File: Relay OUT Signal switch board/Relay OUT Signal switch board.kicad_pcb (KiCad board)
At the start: 2 copper layers, 55 x 75 mm, 18 parts, among them IC1 ULN2003LVDR, J1 1725672, J2 1725672, J3 SE Out, J4 R_Bal_out, J5 Left Bal out, J6 Right 2, J7 Right 1, J8 Left 1, J9 Left 2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

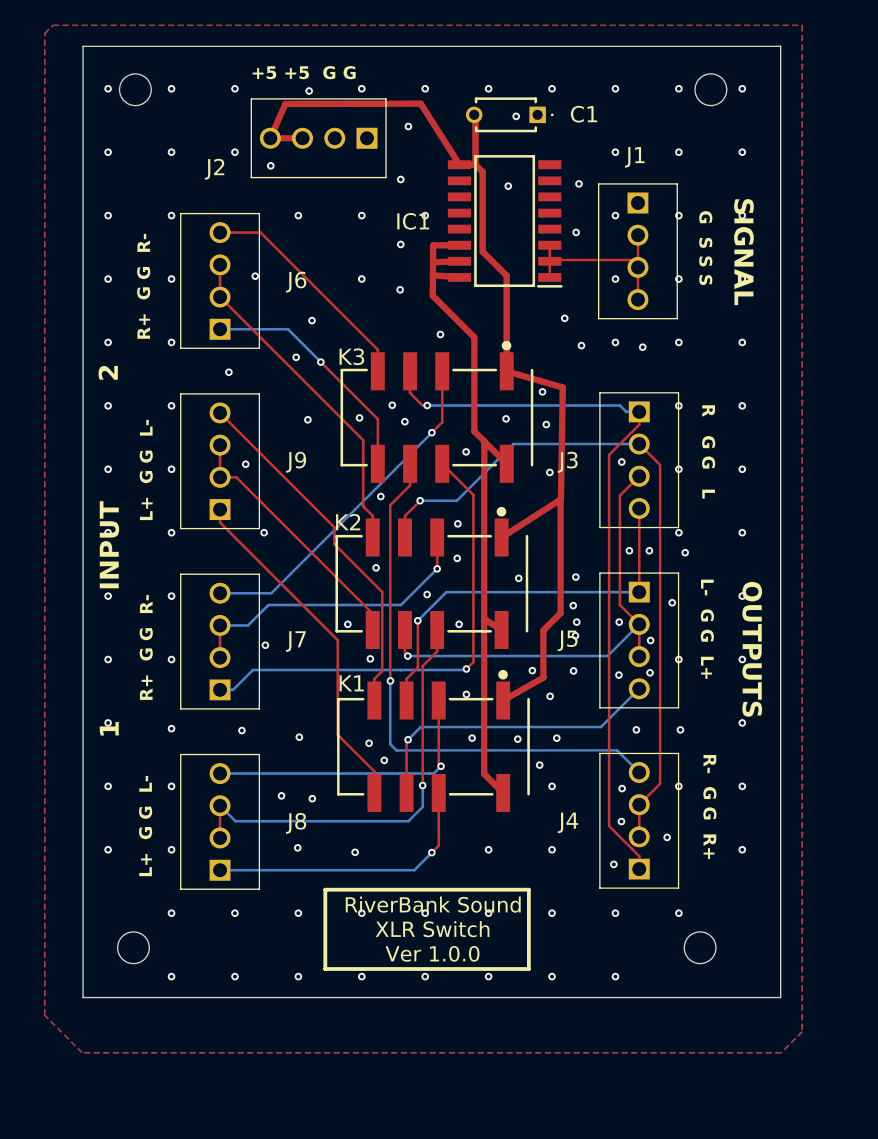
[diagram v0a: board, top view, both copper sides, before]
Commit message: update relayboard set size for RPI4
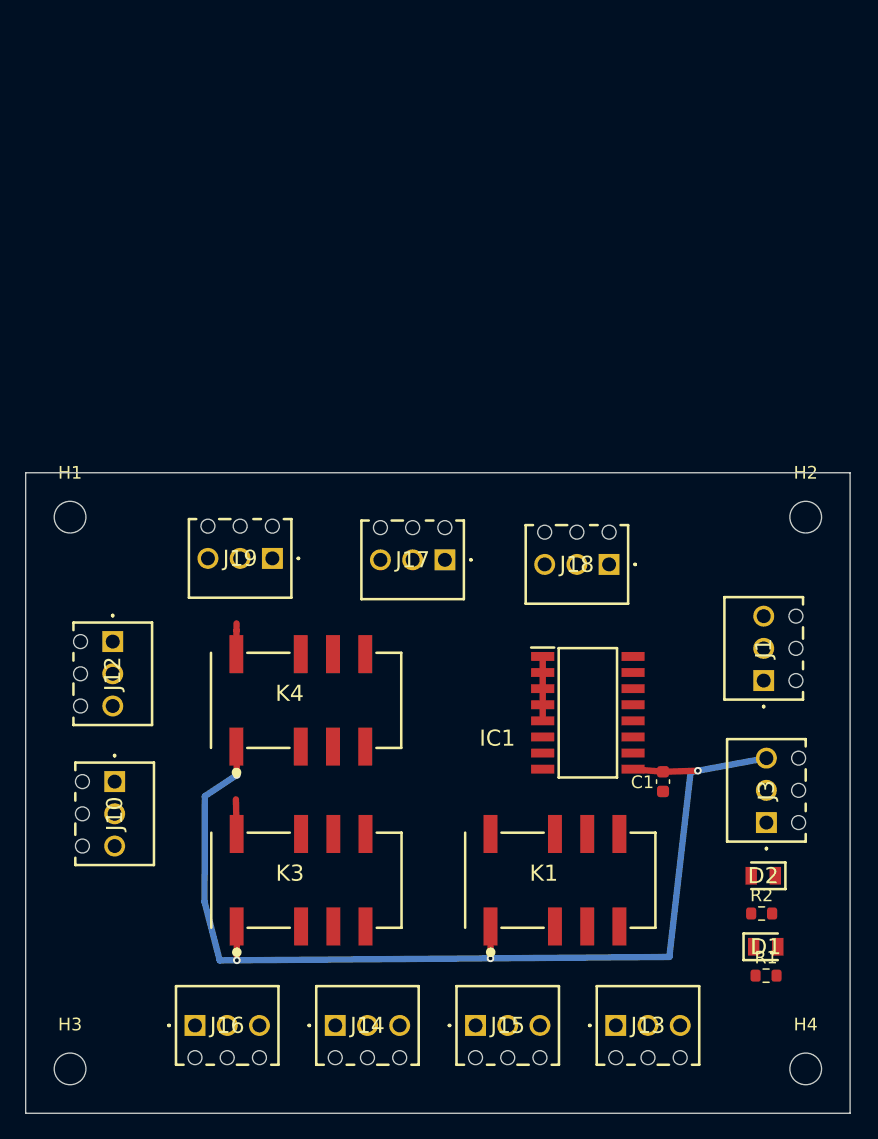
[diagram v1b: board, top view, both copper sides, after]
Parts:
- removed J2: 1725672, samsys:1725672
- removed J4: R_Bal_out, samsys:1725672
- removed J5: Left Bal out, samsys:1725672
- removed J6: Right 2, samsys:1725672
- removed J7: Right 1, samsys:1725672
- removed J8: Left 1, samsys:1725672
- removed J9: Left 2, samsys:1725672
- removed K2: Gnd Relay, samsys:EE2-5NU
- added D1: LS_R976, samsys:LEDC2012X40N, F.Cu at (158.3, 87.4)
- added D2: LS_R976, samsys:LEDC2012X40N, F.Cu at (158.2, 81.8)
- added J10: 1725669, samsys:1725669, F.Cu at (107.0, 74.3)
- added J12: 1725669, samsys:1725669, F.Cu at (106.9, 63.3)
- added J13: 1725669, samsys:1725669, F.Cu at (146.5, 93.6)
- added J14: 1725669, samsys:1725669, F.Cu at (124.4, 93.6)
- added J15: 1725669, samsys:1725669, F.Cu at (135.5, 93.6)
- added J16: 1725669, samsys:1725669, F.Cu at (113.3, 93.6)
- added J17: 1725669, samsys:1725669, F.Cu at (133.1, 56.9)
- added J18: 1725669, samsys:1725669, F.Cu at (146.0, 57.2)
- added J19: 1725669, samsys:1725669, F.Cu at (119.5, 56.8)
- added K4: Left Bal, samsys:EE2-5NU, F.Cu at (114.6, 67.9)
- added R1: 1k, Resistor_SMD:R_0603_1608Metric, F.Cu at (158.4, 89.7)
- added R2: 1k, Resistor_SMD:R_0603_1608Metric, F.Cu at (158.0, 84.8)
- C1: footprint samsys:K104K20X7RK53H5G -> Capacitor_SMD:C_0603_1608Metric
- J1: value 1725672 -> 1725669; footprint samsys:1725672 -> samsys:1725669
- J3: value SE Out -> 1725669; footprint samsys:1725672 -> samsys:1725669
- moved H2 62.7 mm to (161.5, 53.5)
- moved H1 60.7 mm to (103.5, 53.5)
- moved C1 53.5 mm to (150.2, 74.3), turned to 90 degrees
- moved K3 44.4 mm to (114.6, 82.1), turned to 0 degrees
- moved IC1 39.3 mm to (144.3, 68.9), turned to 0 degrees
- moved J1 38.9 mm to (158.2, 66.4), turned to 90 degrees
- moved J3 33.9 mm to (158.4, 77.6), turned to 90 degrees
- moved H4 12.7 mm to (161.5, 97.0)
- moved K1 11.7 mm to (134.7, 82.1), turned to 0 degrees
- moved H3 10.8 mm to (103.5, 97.0)
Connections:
- C1 pad 1: GND -> GND2
- IC1 pad 12: unconnected-(IC1-OUT5-Pad12) -> /switch power
- IC1 pad 13: unconnected-(IC1-OUT4-Pad13) -> /switch power
- IC1 pad 14: Net-(IC1-OUT1) -> /switch power
- IC1 pad 15: Net-(IC1-OUT1) -> /switch power
- IC1 pad 16: Net-(IC1-OUT1) -> /switch power
- IC1 pad 4: unconnected-(IC1-IN4-Pad4) -> Net-(IC1-IN1)
- IC1 pad 5: unconnected-(IC1-IN5-Pad5) -> Net-(IC1-IN1)
- IC1 pad 8: GND -> GND2
- J1 pad 1: GND -> GND2
- J3 pad 1: Net-(J3-Pad1) -> GND2
- J3 pad 2: Net-(J3-Pad2) -> +5V
- J3 pad 3: Net-(J3-Pad3) -> +5V
- K1 pad 2: Net-(J8-Pad4) -> /inp_1_bal_L_-
- K1 pad 3: Net-(J3-Pad4) -> /out_L_-
- K1 pad 4: Net-(J9-Pad4) -> /inp_2_bal_L_-
- K1 pad 5: Net-(J9-Pad1) -> /inp_2_bal_L_+
- K1 pad 6: Net-(J5-Pad4) -> /out_L_+
- K1 pad 7: Net-(J8-Pad1) -> /inp_1_bal_L_+
- K1 pad 8: Net-(IC1-OUT1) -> /switch power
- K3 pad 2: Net-(J7-Pad4) -> /inp_1_bal_R_-
- K3 pad 3: Net-(J3-Pad1) -> /out_R_-
- K3 pad 4: Net-(J6-Pad4) -> /inp_2_bal_R_-
- K3 pad 5: Net-(J6-Pad1) -> /inp_2_bal_R_+
- K3 pad 6: Net-(J4-Pad4) -> /out_R_+
- K3 pad 7: Net-(J7-Pad1) -> /inp_1_bal_R_+
- K3 pad 8: Net-(IC1-OUT1) -> /switch power
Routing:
- net Net-(J3-Pad1): track 58.4 -> 0.00 mm, vias 1 -> 0
- net Net-(IC1-OUT1): track 55.8 -> 0.00 mm
- net Net-(J3-Pad2): track 54.9 -> 0.00 mm, vias 1 -> 0
- net Net-(J4-Pad4): track 43.3 -> 0.00 mm, vias 1 -> 0
- net Net-(J7-Pad1): track 37.5 -> 0.00 mm, vias 1 -> 0
- net Net-(J3-Pad3): track 36.9 -> 0.00 mm, vias 1 -> 0
- net Net-(J8-Pad2): track 33.9 -> 0.00 mm, vias 1 -> 0
- net Net-(J3-Pad4): track 31.7 -> 0.00 mm, vias 1 -> 0
- net Net-(J9-Pad4): track 28.2 -> 0.00 mm
- net Net-(J9-Pad1): track 27.4 -> 0.00 mm
- net Net-(J7-Pad4): track 27.1 -> 0.00 mm, vias 1 -> 0
- net Net-(J6-Pad2): track 26.5 -> 0.00 mm
- net Net-(J5-Pad4): track 24.1 -> 0.00 mm, vias 1 -> 0
- net Net-(J7-Pad2): track 24.0 -> 0.00 mm, vias 1 -> 0
- net Net-(J8-Pad4): track 22.9 -> 0.00 mm, vias 1 -> 0
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- added copper zone on In1.Cu, net GND
- added copper zone on In2.Cu, net GND2
- removed copper zone on B.Cu, net GND
- removed copper zone on F.Cu, net GND
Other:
- board size 55 x 75 mm -> 65 x 50.5 mm
- copper layers 2 -> 4
- board text removed: "+5 +5 G G"
- board text removed: "1"
- board text removed: "2"
- board text removed: "G S S S"
- board text removed: "INPUT"
- board text removed: "L+ G G L-"
- board text removed: "L- G G L+"
- board text removed: "OUTPUTS"
- board text removed: "R G G L"
- board text removed: "R+ G G R-"
- board text removed: "R- G G R+"
- board text removed: "RiverBank Sound XLR Switch Ver 1.0.0"
- board text removed: "SIGNAL"

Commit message: add updates to se to diff
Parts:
- moved D2 52.4 mm to (144.4, 31.2)
- moved R1 52.4 mm to (144.7, 39.1)
- moved D1 52.4 mm to (144.6, 36.8)
- moved R2 52.4 mm to (144.3, 34.2)
- moved J1 43.0 mm to (125.5, 38.4)
- moved J3 43.0 mm to (125.8, 49.6)
- moved J19 41.3 mm to (160.0, 64.4), turned to 90 degrees
- moved J18 35.4 mm to (160.0, 89.8), turned to 90 degrees
- moved J17 33.6 mm to (159.9, 77.1), turned to 90 degrees
- moved IC1 31.4 mm to (155.9, 39.8)
- moved C1 31.4 mm to (161.8, 45.2)
- moved K3 19.3 mm to (130.6, 71.2), turned to -90 degrees
- moved K1 13.8 mm to (143.0, 71.2), turned to -90 degrees
- moved K4 12.1 mm to (121.3, 57.9), turned to -90 degrees
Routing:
- net +5V: track 84.9 -> 0.00 mm, vias 4 -> 0
- net /switch power: track 5.16 -> 0.00 mm
- net Net-(IC1-IN1): track 5.08 -> 0.00 mm

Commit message: updated final four boards for streamer
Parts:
- removed K4: Left Bal, samsys:EE2-5NU
- added J2: Conn_01x01_Socket, Connector_PinHeader_1.00mm:PinHeader_1x01_P1.00mm_Vertical, F.Cu at (162.7, 72.2)
- added K2: EC2-5SNU, Relay_THT:Relay_DPDT_Kemet_EC2, F.Cu at (125.9, 68.5)
- added R3: 10R, Resistor_SMD:R_0603_1608Metric, F.Cu at (145.6, 59.4)
- IC1: footprint samsys:SOIC127P780X200-16N -> samsys:SOIC127P600X175-16N
- K1: value Left Bal -> EC2-5SNU; footprint samsys:EE2-5NU -> Relay_THT:Relay_DPDT_Kemet_EC2
- K3: value Right Bal -> EC2-5SNU; footprint samsys:EE2-5NU -> Relay_THT:Relay_DPDT_Kemet_EC2
- moved J1 56.7 mm to (158.0, 85.0)
- moved J19 44.1 mm to (116.6, 56.5), turned to 180 degrees
- moved J18 38.8 mm to (139.6, 56.7), turned to 180 degrees
- moved J17 37.8 mm to (128.1, 56.6), turned to 180 degrees
- moved D2 36.2 mm to (160.9, 63.5)
- moved R2 36.2 mm to (160.8, 66.5), turned to 180 degrees
- moved IC1 30.7 mm to (152.5, 70.3), turned to 180 degrees
- moved J3 29.7 mm to (154.6, 56.7), turned to 180 degrees
- moved D1 26.9 mm to (161.0, 58.2)
- moved R1 26.7 mm to (160.6, 60.5)
- moved C1 20.6 mm to (152.2, 63.4), turned to 180 degrees
- moved K3 16.4 mm to (114.4, 68.5), turned to 0 degrees
- moved J12 13.5 mm to (106.7, 76.8)
- moved J10 9.16 mm to (106.6, 65.2)
- moved K1 6.93 mm to (136.6, 68.5), turned to 0 degrees
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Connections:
- net GND renamed /sig ground
- D2 pad 1: unconnected-(D2-K-Pad1) -> Net-(D2-K)
- J10 pad 1: /SE_1_R -> /SE_1_L
- J10 pad 3: /SE_1_L -> /SE_1_R
- J12 pad 1: /SE_2_R -> /SE_2_L
- J12 pad 3: /SE_2_L -> /SE_2_R
- J13 pad 1: /inp_2_bal_L_+ -> /inp_2_bal_L_-
- J13 pad 3: /inp_2_bal_L_- -> /inp_2_bal_L_+
- J14 pad 1: /inp_2_bal_R_+ -> /inp_2_bal_R_-
- J14 pad 3: /inp_2_bal_R_- -> /inp_2_bal_R_+
- J15 pad 1: /inp_1_bal_L_+ -> /inp_1_bal_L_-
- J15 pad 3: /inp_1_bal_L_- -> /inp_1_bal_L_+
- J16 pad 1: /inp_1_bal_R_+ -> /inp_1_bal_R_-
- J16 pad 3: /inp_1_bal_R_- -> /inp_1_bal_R_+
- J17 pad 1: /out_R_- -> /out_R_+
- J17 pad 3: /out_R_+ -> /out_R_-
- J18 pad 1: /out_L_- -> /out_L_+
- J18 pad 3: /out_L_+ -> /out_L_-
- J19 pad 1: /SE_OUT_L -> /SE_OUT_R
- J19 pad 3: /SE_OUT_R -> /SE_OUT_L
- K1 pad 3: /out_L_- -> /inp_1_bal_L_-
- K1 pad 4: /inp_2_bal_L_- -> /out_L_-
- K1 pad 5: /inp_2_bal_L_+ -> /inp_2_bal_L_-
- K1 pad 8: /switch power -> /inp_2_bal_L_+
- K3 pad 3: /out_R_- -> /SE_1_L
- K3 pad 4: /inp_2_bal_R_- -> /SE_OUT_L
- K3 pad 5: /inp_2_bal_R_+ -> /SE_2_L
- K3 pad 8: /switch power -> /SE_2_R
- R2 pad 1: unconnected-(R2-Pad1) -> Net-(D2-K)
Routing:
- net +5V: track 0.00 -> 70.5 mm, vias 0 -> 2
- net /switch power: track 0.00 -> 56.4 mm, vias 0 -> 2
- net /inp_1_bal_R_-: track 0.00 -> 26.3 mm
- net /inp_1_bal_R_+: track 0.00 -> 26.1 mm
- net /SE_OUT_R: track 0.00 -> 23.3 mm
- net /SE_OUT_L: track 0.00 -> 23.0 mm
- net /out_R_+: track 0.00 -> 22.8 mm
- net /out_R_-: track 0.00 -> 22.7 mm
- net /out_L_-: track 0.00 -> 22.2 mm
- net /out_L_+: track 0.00 -> 21.8 mm
- net /inp_1_bal_L_+: track 0.00 -> 21.0 mm
- net /inp_1_bal_L_-: track 0.00 -> 21.0 mm
- net /inp_2_bal_L_-: track 0.00 -> 17.8 mm
- net /inp_2_bal_L_+: track 0.00 -> 17.4 mm
- net /inp_2_bal_R_-: track 0.00 -> 16.6 mm
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- added copper zone on B.Cu, net Earth
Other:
- copper layers 4 -> 6
- board text added: "5V 5V G"
- board text added: "Input"
- board text added: "L G R"
- board text added: "L G R (1)"
- board text added: "L G R (2)"
- board text added: "L- G L+"
- board text added: "R- G R+"
- board text added: "Relay G"
- board text added: "Riverbank systems - relay - version 0.1"
- board text added: "chan 1"
- board text added: "chan 2"

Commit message: More changes to the boards
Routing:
- net /switch power: track 56.4 -> 39.4 mm, vias 2 -> 1
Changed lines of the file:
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@@
 			(layer "F.Fab")
-		)
-		(fp_text user "${REFERENCE}"
-			(at 0 0 180)
-			(layer "F.Fab")
-			(effects
-				(font
-					(size 1.27 1.27)
-					(thickness 0.254)
-				)
-			)
 		)
 		(pad "1" smd rect
@@
 	)
 	(segment
-		(start 157.425 63.525)
-		(end 159.95 63.5)
-		(width 0.5)
-		(layer "F.Cu")
-		(net 29)
-	)
-	(segment
 		(start 145.45 69.6)
 		(end 149.725 69.635)
@@
 		(width 0.5)
 		(layer "F.Cu")
-		(net 29)
-	)
-	(via
-		(at 157.425 63.525)
-		(size 0.6)
-		(drill 0.3)
-		(layers "F.Cu" "B.Cu")
 		(net 29)
 	)
@@
 	)
 	(segment
-		(start 152.15 67.325)
-		(end 155.95 63.525)
-		(width 0.5)
-		(layer "In3.Cu")
-		(net 29)
-	)
-	(segment
 		(start 141.675 70.068196)
 		(end 144.975 70.075)
@@
 	)
 	(segment
-		(start 147.725 67.325)
-		(end 152.15 67.325)
-		(width 0.5)
-		(layer "In3.Cu")
-		(net 29)
-	)
-	(segment
 		(start 119.525 68.465)
 		(end 120.725 70.025)
@@
 		(width 0.5)
 		(layer "In3.Cu")
-		(net 29)
-	)
-	(segment
-		(start 145.45 69.6)
-		(end 147.725 67.325)
-		(width 0.5)
-		(layer "In3.Cu")
-		(net 29)
-	)
-	(segment
-		(start 155.95 63.525)
-		(end 157.425 63.525)
-		(width 0.5)
-		(layer "In3.Cu")
